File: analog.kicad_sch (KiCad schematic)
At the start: 27 parts, among them J2 ATX, J3 Conn_01x05, Q1 IRF3205, U1 LM358, U1 TL494, U2 LM358

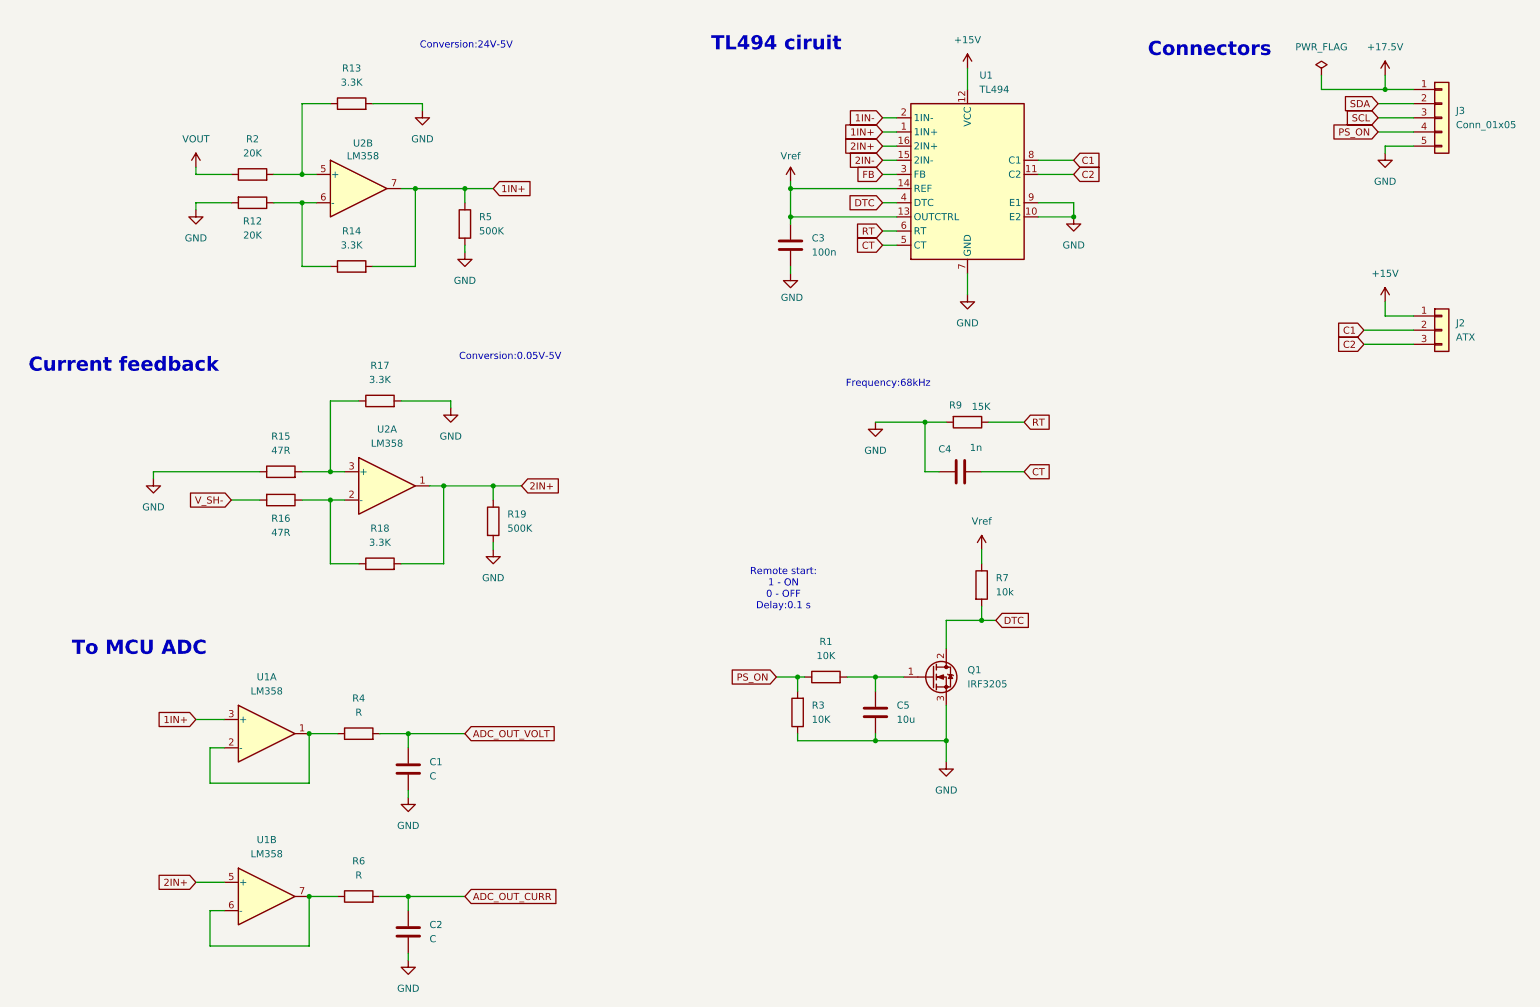
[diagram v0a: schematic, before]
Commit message: added: RC calculation,connectors Vin/Vmeas
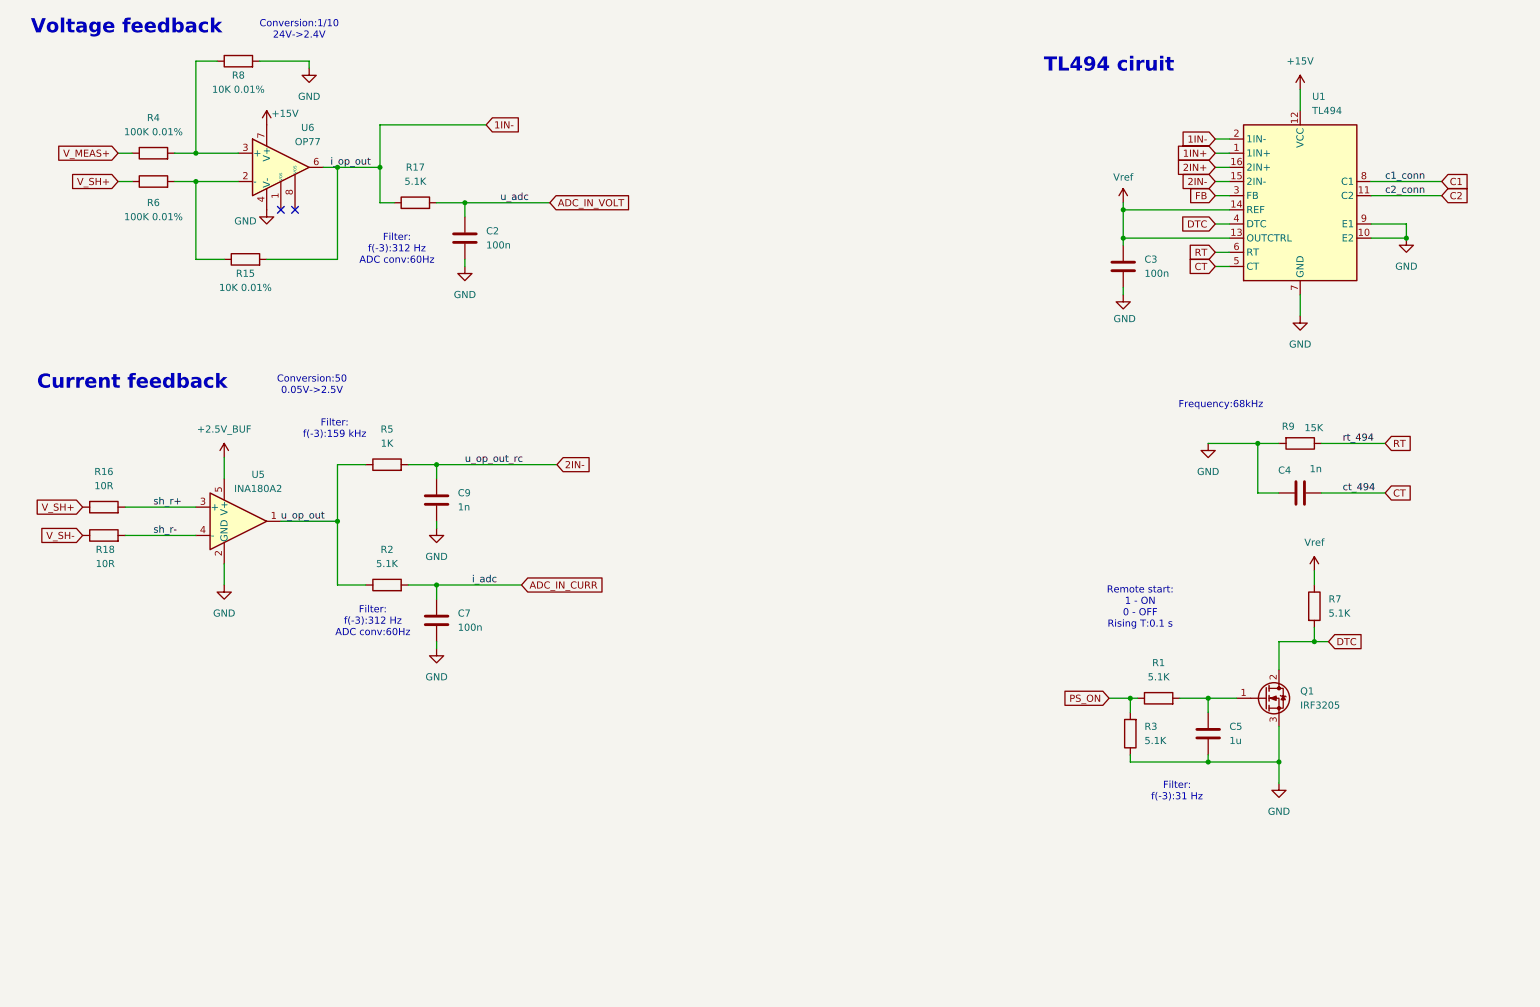
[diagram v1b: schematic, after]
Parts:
- removed C1: C, symbol Device:C
- removed J2: ATX, symbol Connector_Generic:Conn_01x03
- removed J3: Conn_01x05, symbol Connector_Generic:Conn_01x05
- removed R12: 20K, symbol Device:R
- removed R13, R14: 3.3K, symbol Device:R
- removed R19: 500K, symbol Device:R
- removed U1, U2: LM358, symbol Amplifier_Operational:LM358
- removed unit 2 of U1
- added C7: 100n, symbol Device:C
- added C9: 1n, symbol Device:C
- added R8: 10K 0.01%, symbol Device:R
- added U5: INA180A2, Package_TO_SOT_SMD:SOT-23-5, symbol Amplifier_Current:INA180A2
- added U6: OP77, Package_SO:SOIC-8_3.9x4.9mm_P1.27mm, symbol Amplifier_Operational:OP77
- C2: value C -> 100n
- C5: value 10u -> 1u
- R1, R3: value 10K -> 5.1K
- R15: value 47R -> 10K 0.01%
- R16: value 47R -> 10R
- R17: value 3.3K -> 5.1K
- R18: value 3.3K -> 10R
- R2: value 20K -> 5.1K
- R4, R6: value R -> 100K 0.01%
- R5: value 500K -> 1K
- R7: value 10k -> 5.1K
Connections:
- net +15V: now also U6.7 (V+)
- net 1IN+: no longer R5.1
- net 1IN-: now also R15.2, R17.1, U6.6
- net 2IN+: no longer R18.2
- net 2IN-: now also R5.2, C9.1
- net GND: now also C7.2, C9.2, R8.2, U5.2 (GND), U6.4 (V-); no longer R15.1, R17.2, R5.2
- net V_SH-: now also R18.1; no longer R16.2
- net ADC_IN_CURR: now reaches R2.2
- net ADC_IN_CURR: now also C7.1
- net V_SH+: now reaches R16.1
- net V_SH+: now also R6.1; no longer R18.1
- net V_MEAS+: now reaches R4.1
- net ADC_OUT_CURR: no longer names the net of R6.2
- net ADC_OUT_CURR: now also R15.1, U6.2 (-); no longer C2.1
- net ADC_OUT_VOLT: no longer names the net of R4.2
- net ADC_OUT_VOLT: now also R8.1, U6.3 (+)
- net VOUT renamed u_op_out
- net u_op_out: now also R5.1, U5.1
- new net +2.5V_BUF: U5.5 (V+)
- new net ADC_IN_VOLT: C2.1, R17.2
- new net sh_r+: R16.2, U5.3 (+)
- new net sh_r-: R18.2, U5.4 (-)
- no-connect marks 0 -> 2
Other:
- note added: "Conversion:1/10 24V->2.4V"
- note added: "Conversion:50 0.05V->2.5V"
- note added: "Filter: f(-3):159 kHz"
- note added: "Filter: f(-3):31 Hz"
- note added: "Filter: f(-3):312 Hz ADC conv:60Hz"
- note added: "Remote start: 1 - ON 0 - OFF Rising T:0.1 s"
- note added: "Voltage feedback"
- note removed: "Connectors"
- note removed: "Conversion:0.05V-5V"
- note removed: "Conversion:24V-5V"
- note removed: "Remote start: 1 - ON 0 - OFF Delay:0.1 s"
- note removed: "To MCU ADC"
- moved on the sheet: C3, C4, C5, Q1, R1, R3, R7, R9, U1

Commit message: new OpAmp, new RC calc, G431 added
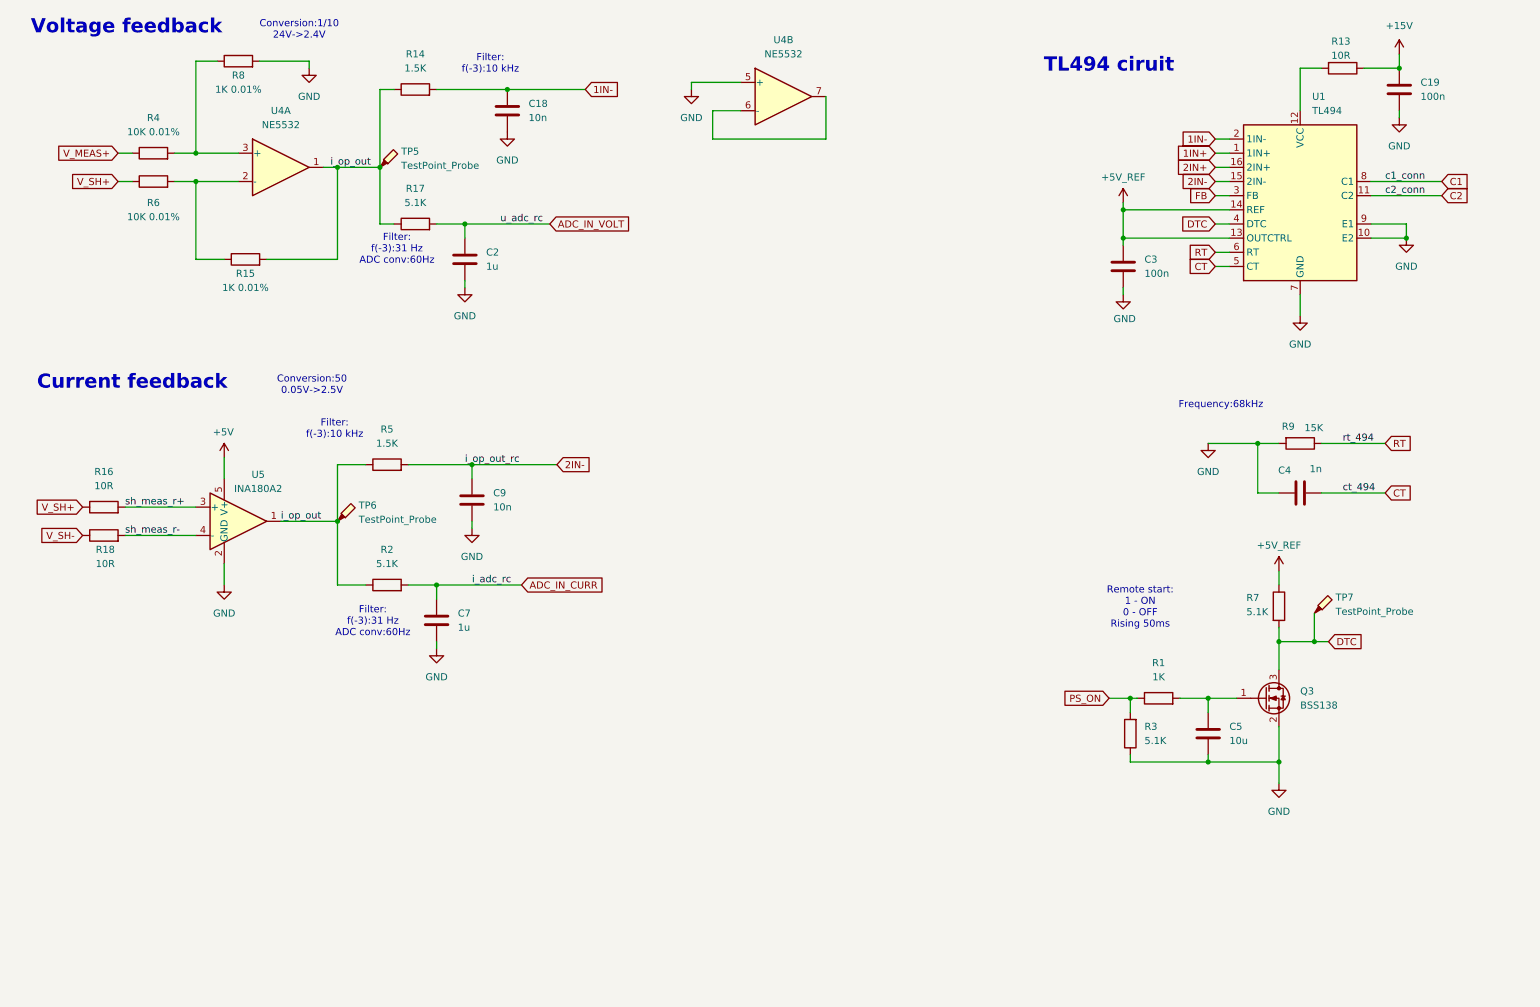
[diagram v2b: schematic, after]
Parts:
- removed Q1: IRF3205, symbol Transistor_FET:IRF3205
- removed U6: OP77, Package_SO:SOIC-8_3.9x4.9mm_P1.27mm, symbol Amplifier_Operational:OP77
- added C18: 10n, symbol Device:C
- added C19: 100n, symbol Device:C
- added Q3: BSS138, Package_TO_SOT_SMD:SOT-23, symbol Transistor_FET:BSS138
- added R13: 10R, symbol Device:R
- added R14: 1.5K, symbol Device:R
- added TP5, TP6, TP7: TestPoint_Probe, symbol Connector:TestPoint_Probe
- added U4: NE5532, Package_SO:SOIC-8_3.9x4.9mm_P1.27mm, symbol Amplifier_Operational:NE5532
- C2, C7: value 100n -> 1u
- C5: value 1u -> 10u
- C9: value 1n -> 10n
- R1: value 5.1K -> 1K
- R15, R8: value 10K 0.01% -> 1K 0.01%
- R4, R6: value 100K 0.01% -> 10K 0.01%
- R5: value 1K -> 1.5K
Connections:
- net +15V: now also C19.1, R13.1; no longer U1.12 (VCC)
- net 1IN-: now also C18.1, R14.2; no longer R15.2, R17.1
- net DTC: now also Q3.3 (D), TP7.1
- net GND: now also C18.2, C19.2, Q3.2 (S), U4.5 (+)
- net at C5.1, R1.2: now also Q3.1 (G)
- net at R15.1, R6.2: now also U4.2 (-)
- net at R4.2, R8.1: now also U4.3 (+)
- net +2.5V_BUF renamed +5V
- net Vref renamed +5V_REF
- net sh_r+ renamed sh_meas_r+
- net sh_r- renamed sh_meas_r-
- net u_op_out renamed i_op_out
- net i_op_out: now also R15.2, R17.1, R14.1, TP5.1, TP6.1, U4.1
- new net: R13.2, U1.12 (VCC)
- new net: U4.6 (-), U4.7
- no-connect marks 2 -> 0
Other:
- note added: "Filter: f(-3):10 kHz"
- note added: "Filter: f(-3):31 Hz ADC conv:60Hz"
- note added: "Remote start: 1 - ON 0 - OFF Rising 50ms"
- note removed: "Filter: f(-3):159 kHz"
- note removed: "Filter: f(-3):31 Hz"
- note removed: "Filter: f(-3):312 Hz ADC conv:60Hz"
- note removed: "Remote start: 1 - ON 0 - OFF Rising T:0.1 s"
- moved on the sheet: C2, C9, R17, R7

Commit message: MCU analog perephery, TL494 FB wiring
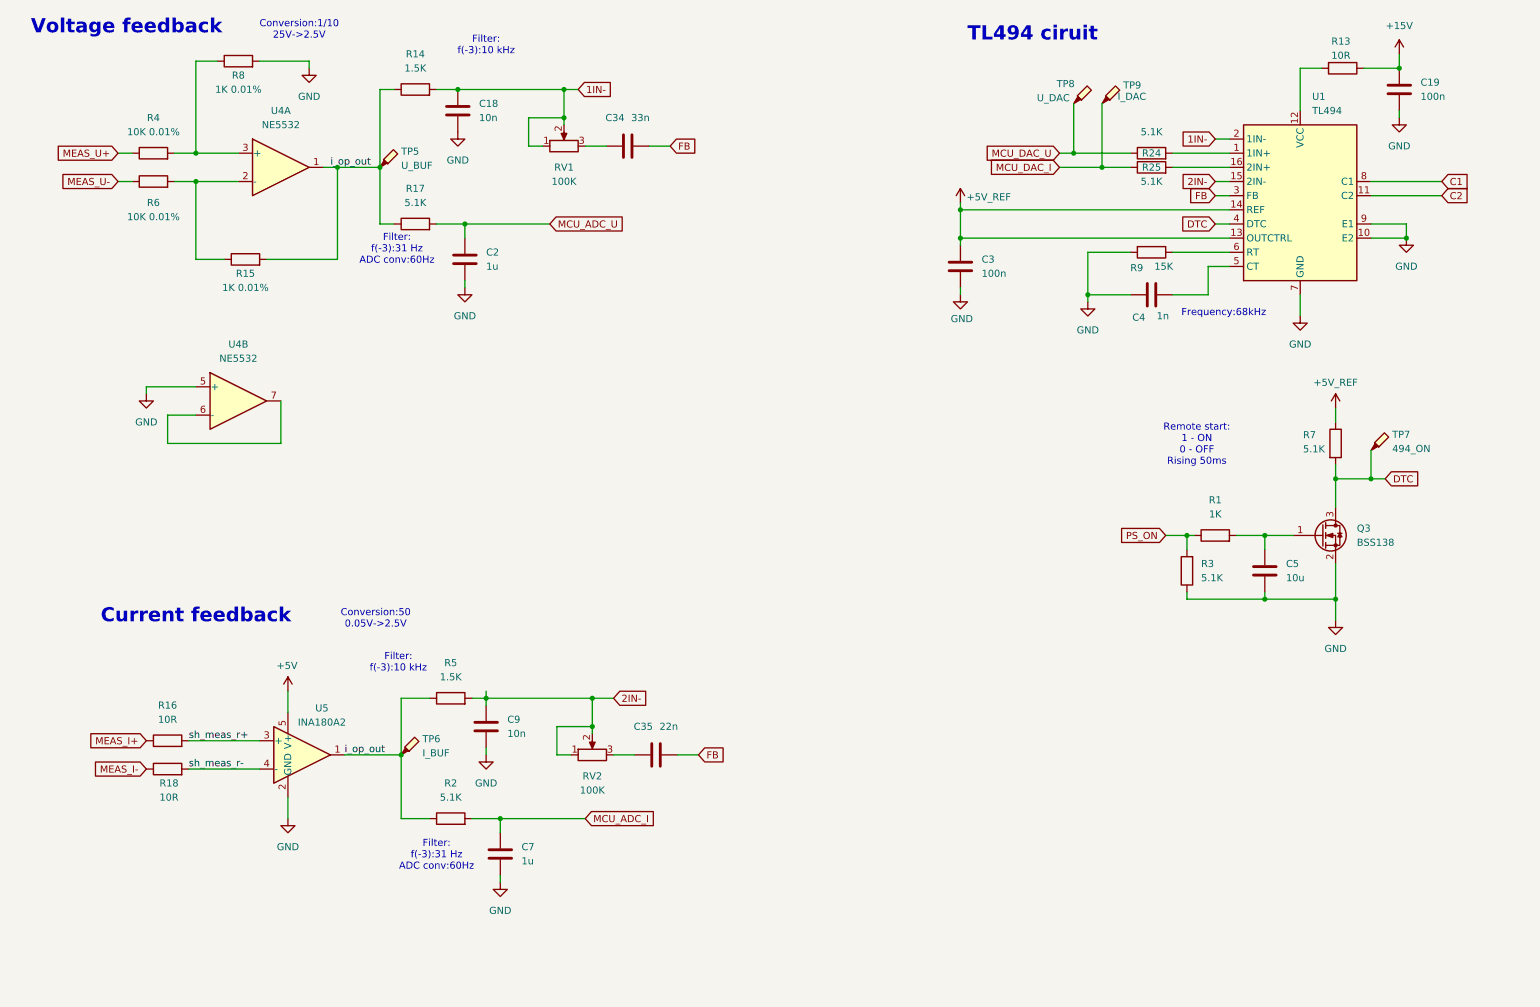
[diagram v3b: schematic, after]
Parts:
- added C34: 33n, symbol Device:C
- added C35: 22n, symbol Device:C
- added R24, R25: 5.1K, symbol Device:R
- added RV1, RV2: 100K, symbol Device:R_Potentiometer
- added TP8: U_DAC, symbol Connector:TestPoint_Probe
- added TP9: I_DAC, symbol Connector:TestPoint_Probe
- TP5: value TestPoint_Probe -> U_BUF
- TP6: value TestPoint_Probe -> I_BUF
- TP7: value TestPoint_Probe -> 494_ON
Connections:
- net 1IN-: now also RV1.1, RV1.2
- net 2IN-: now also RV2.1, RV2.2
- net FB: now also C34.2, C35.2
- net 1IN+: no longer names the net of U1.1 (1IN+)
- net 1IN+: now also R24.2
- net 2IN+: no longer names the net of U1.16 (2IN+)
- net 2IN+: now also R25.2
- net ADC_IN_CURR renamed MCU_ADC_I
- net ADC_IN_VOLT renamed MCU_ADC_U
- net CT: no longer names the net of C4.2, U1.5 (CT)
- net RT: no longer names the net of R9.1, U1.6 (RT)
- net V_MEAS+ renamed MEAS_U+
- net V_SH+ renamed MEAS_I+
- net MEAS_I+: no longer R6.1
- net V_SH- renamed MEAS_I-
- new net: C34.1, RV1.3
- new net: C35.1, RV2.3
- new net MCU_DAC_I: R25.1, TP9.1
- new net MCU_DAC_U: R24.1, TP8.1
- new net MEAS_U-: R6.1
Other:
- note added: "Conversion:1/10 25V->2.5V"
- note removed: "Conversion:1/10 24V->2.4V"
- moved on the sheet: C18, C3, C4, C5, C7, C9, Q3, R1, R16, R18, R2, R3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

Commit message: assign footprints
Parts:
- C18, C2, C34, C35, C4, C5, C7, C9: footprint (none) -> Capacitor_SMD:C_1206_3216Metric_Pad1.33x1.80mm_HandSolder
- C19, C3: footprint (none) -> Capacitor_SMD:C_0805_2012Metric_Pad1.18x1.45mm_HandSolder
- R1, R13, R14, R15, R16, R18, R4, R5, R6, R8, R9: footprint (none) -> Resistor_SMD:R_1206_3216Metric_Pad1.30x1.75mm_HandSolder
- R17, R2, R24, R25, R3, R7: footprint (none) -> Resistor_SMD:R_0805_2012Metric_Pad1.20x1.40mm_HandSolder
- RV1, RV2: footprint (none) -> Potentiometer_THT:Potentiometer_Bourns_3299W_Vertical
- TP5, TP6, TP7, TP8, TP9: footprint (none) -> TestPoint:TestPoint_Pad_D2.0mm
- U1: footprint (none) -> Package_SO:SOIC-16_3.9x9.9mm_P1.27mm
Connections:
- net MEAS_I- is gone; now on net GND: R18.1
- net MEAS_U- is gone; now on net MEAS_I+: R6.1
- net +15V: no longer C19.1
- net i_op_out: no longer R14.1, R15.2, R17.1, TP5.1, U4.1
- net at R13.2, U1.12 (VCC): now also C19.1
- net 1IN- renamed U_1IN-
- net 2IN- renamed I_2IN-
- net MEAS_U+ renamed VOUT
- net PS_ON renamed MCU_494_ON
- new net: R14.1, R15.2, R17.1, TP5.1, U4.1
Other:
- moved on the sheet: C19, R13
